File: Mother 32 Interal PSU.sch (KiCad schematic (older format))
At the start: 15 parts, among them P1 CONN_01X02, P2 CONN_02X08, P3 CONN_02X08, P4 CONN_02X08, P5 CONN_02X08, P6 CONN_02X08, P7 CONN_02X08, P8 CONN_02X08, P9 CONN_02X08, U1 BPM15, U2 R-78E5.0-0.5

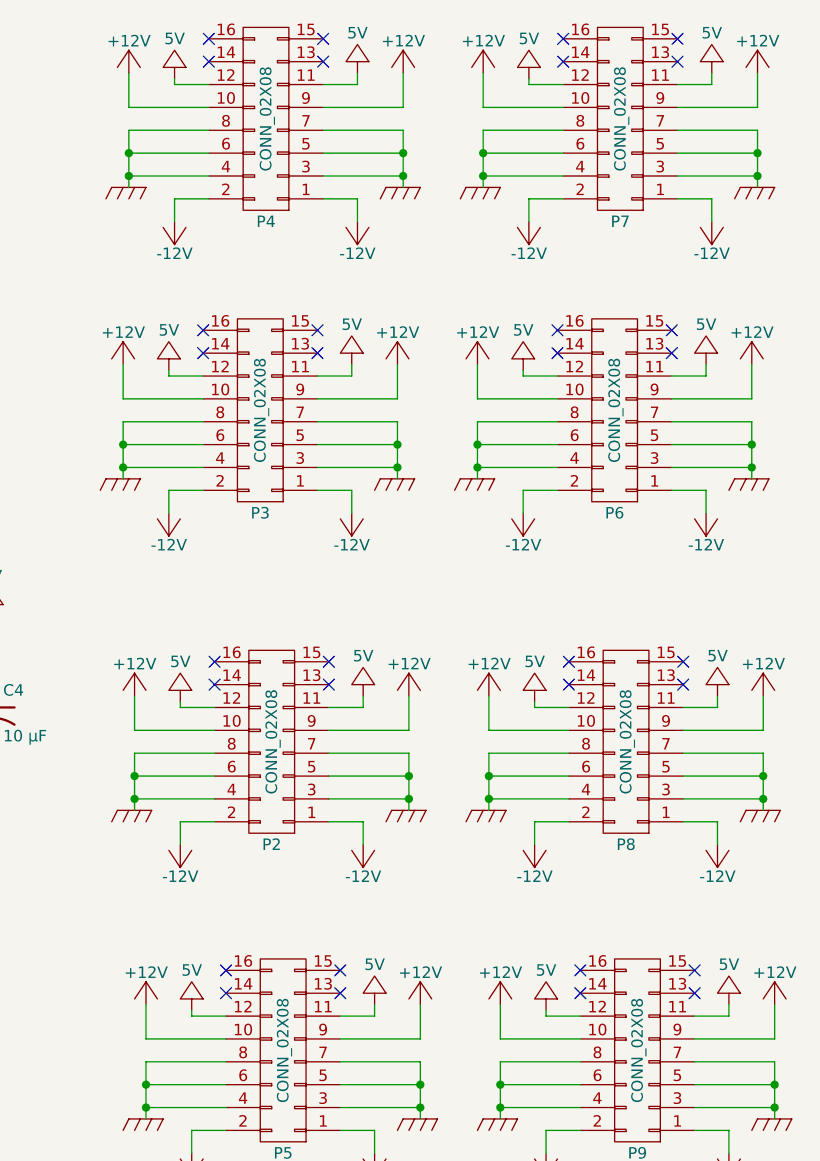
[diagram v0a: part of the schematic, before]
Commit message: updated ground planes and power traces, added CV/GATE connections
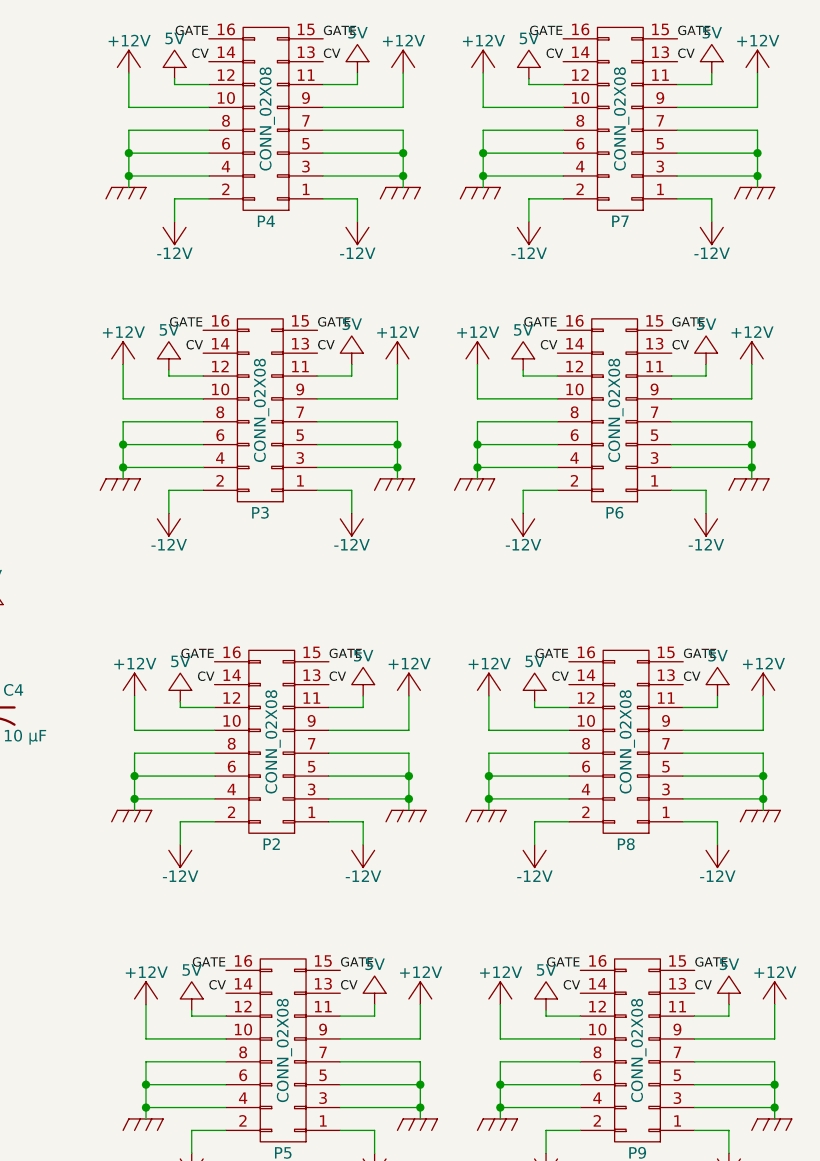
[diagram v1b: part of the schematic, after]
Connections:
- net CV: now reaches P2.13 (P13)
- net CV: now also P2.14 (P14), P3.13 (P13), P3.14 (P14), P4.13 (P13), P4.14 (P14), P5.13 (P13), P5.14 (P14), P6.13 (P13), P6.14 (P14), P7.13 (P13), P7.14 (P14), P8.13 (P13), P8.14 (P14), P9.13 (P13), P9.14 (P14)
- net GATE: now reaches P2.15 (P15)
- net GATE: now also P2.16 (P16), P3.15 (P15), P3.16 (P16), P4.15 (P15), P4.16 (P16), P5.15 (P15), P5.16 (P16), P6.15 (P15), P6.16 (P16), P7.15 (P15), P7.16 (P16), P8.15 (P15), P8.16 (P16), P9.15 (P15), P9.16 (P16)
- no-connect marks 32 -> 0
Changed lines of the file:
@@
 LIBS:valves
 LIBS:MySynthParts
+LIBS:Mother 32 Interal PSU-cache
 EELAYER 25 0
 EELAYER END
@@
 	1    0    0    -1
 $EndComp
-NoConn ~ 6575 3525
-NoConn ~ 6575 3625
-NoConn ~ 7075 3525
-NoConn ~ 7075 3625
 Wire Wire Line
 	6425 3700 6425 3725
@@
 	1    0    0    -1
 $EndComp
-NoConn ~ 8125 3525
-NoConn ~ 8125 3625
-NoConn ~ 8625 3525
-NoConn ~ 8625 3625
 Wire Wire Line
 	7975 3700 7975 3725
@@
 	1    0    0    -1
 $EndComp
-NoConn ~ 6525 2075
-NoConn ~ 6525 2175
-NoConn ~ 7025 2075
-NoConn ~ 7025 2175
 Wire Wire Line
 	6375 2250 6375 2275
@@
 	1    0    0    -1
 $EndComp
-NoConn ~ 8075 2075
-NoConn ~ 8075 2175
-NoConn ~ 8575 2075
-NoConn ~ 8575 2175
 Wire Wire Line
 	7925 2250 7925 2275
@@
 	1    0    0    -1
 $EndComp
-NoConn ~ 6625 4875
-NoConn ~ 6625 4975
-NoConn ~ 7125 4875
-NoConn ~ 7125 4975
 Wire Wire Line
 	6475 5050 6475 5075
@@
 	1    0    0    -1
 $EndComp
-NoConn ~ 8175 4875
-NoConn ~ 8175 4975
-NoConn ~ 8675 4875
-NoConn ~ 8675 4975
 Wire Wire Line
 	8025 5050 8025 5075
@@
 	1    0    0    -1
 $EndComp
-NoConn ~ 6550 800
-NoConn ~ 6550 900
-NoConn ~ 7050 800
-NoConn ~ 7050 900
 Wire Wire Line
 	6400 975  6400 1000
@@
 	1    0    0    -1
 $EndComp
-NoConn ~ 8100 800
-NoConn ~ 8100 900
-NoConn ~ 8600 800
-NoConn ~ 8600 900
 Wire Wire Line
 	7950 975  7950 1000
@@
 Wire Wire Line
 	8750 1500 8600 1500
+Text Label 7050 800  0    40   ~ 0
+GATE
+Text Label 6550 800  2    40   ~ 0
+GATE
+Text Label 8100 800  2    40   ~ 0
+GATE
+Text Label 8600 800  0    40   ~ 0
+GATE
+Text Label 6525 2075 2    40   ~ 0
+GATE
+Text Label 7025 2075 0    40   ~ 0
+GATE
+Text Label 8575 2075 0    40   ~ 0
+GATE
+Text Label 8075 2075 2    40   ~ 0
+GATE
+Text Label 6575 3525 2    40   ~ 0
+GATE
+Text Label 7075 3525 0    40   ~ 0
+GATE
+Text Label 8625 3525 0    40   ~ 0
+GATE
+Text Label 8125 3525 2    40   ~ 0
+GATE
+Text Label 6625 4875 2    40   ~ 0
+GATE
+Text Label 7125 4875 0    40   ~ 0
+GATE
+Text Label 8675 4875 0    40   ~ 0
+GATE
+Text Label 8175 4875 2    40   ~ 0
+GATE
+Text Label 6625 4975 2    40   ~ 0
+CV
+Text Label 7125 4975 0    40   ~ 0
+CV
+Text Label 8675 4975 0    40   ~ 0
+CV
+Text Label 8175 4975 2    40   ~ 0
+CV
+Text Label 6575 3625 2    40   ~ 0
+CV
+Text Label 7075 3625 0    40   ~ 0
+CV
+Text Label 8125 3625 2    40   ~ 0
+CV
+Text Label 8625 3625 0    40   ~ 0
+CV
+Text Label 8575 2175 0    40   ~ 0
+CV
+Text Label 8075 2175 2    40   ~ 0
+CV
+Text Label 7025 2175 0    40   ~ 0
+CV
+Text Label 6525 2175 2    40   ~ 0
+CV
+Text Label 8600 900  0    40   ~ 0
+CV
+Text Label 8100 900  2    40   ~ 0
+CV
+Text Label 7050 900  0    40   ~ 0
+CV
+Text Label 6550 900  2    40   ~ 0
+CV
 $EndSCHEMATC

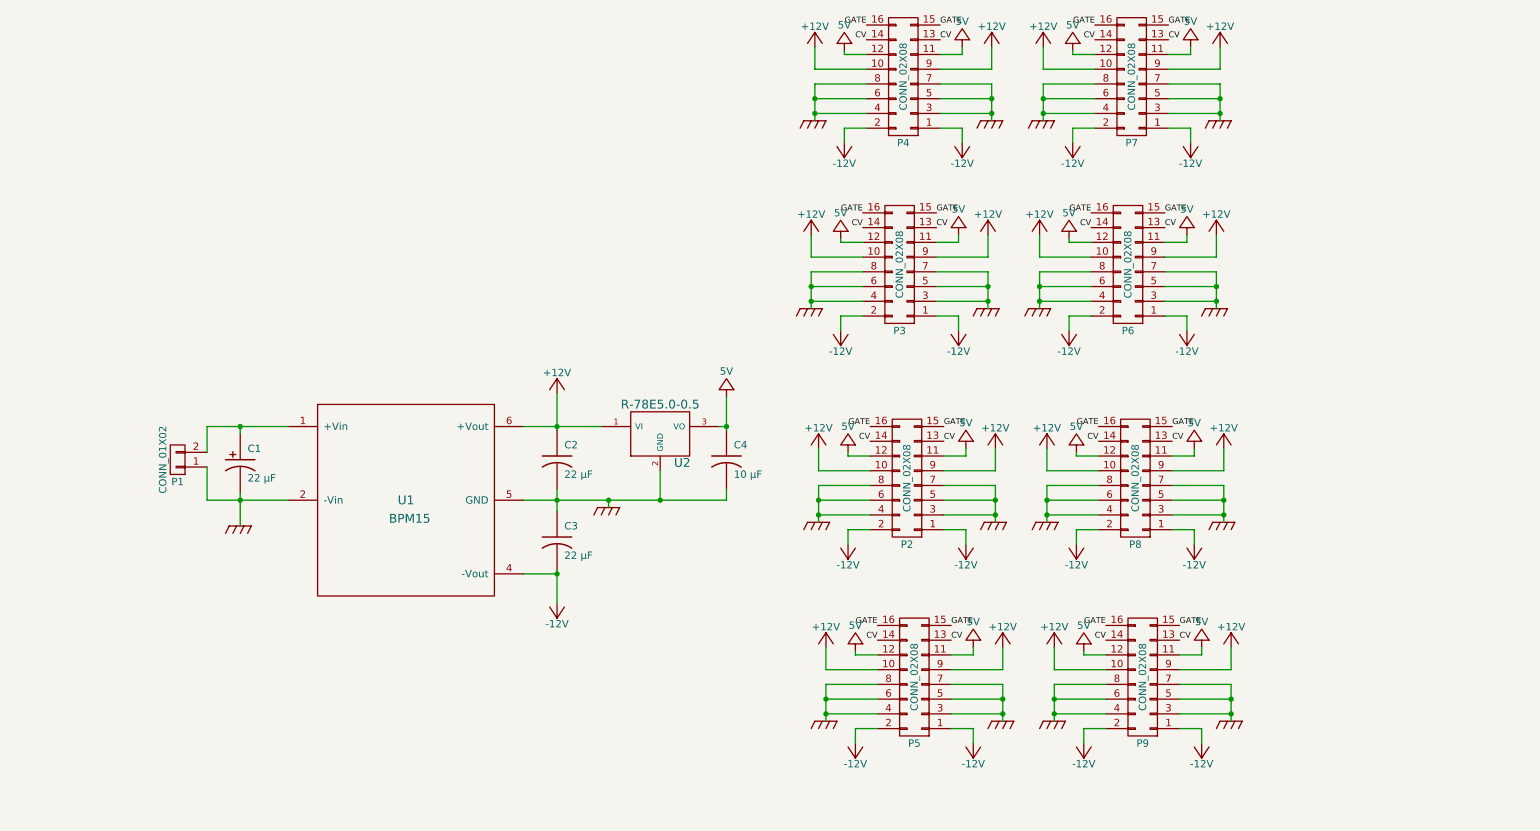
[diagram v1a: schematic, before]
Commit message: first commit with LDOs but these things will just get too damn hot, so will now revert to just LC filter on output
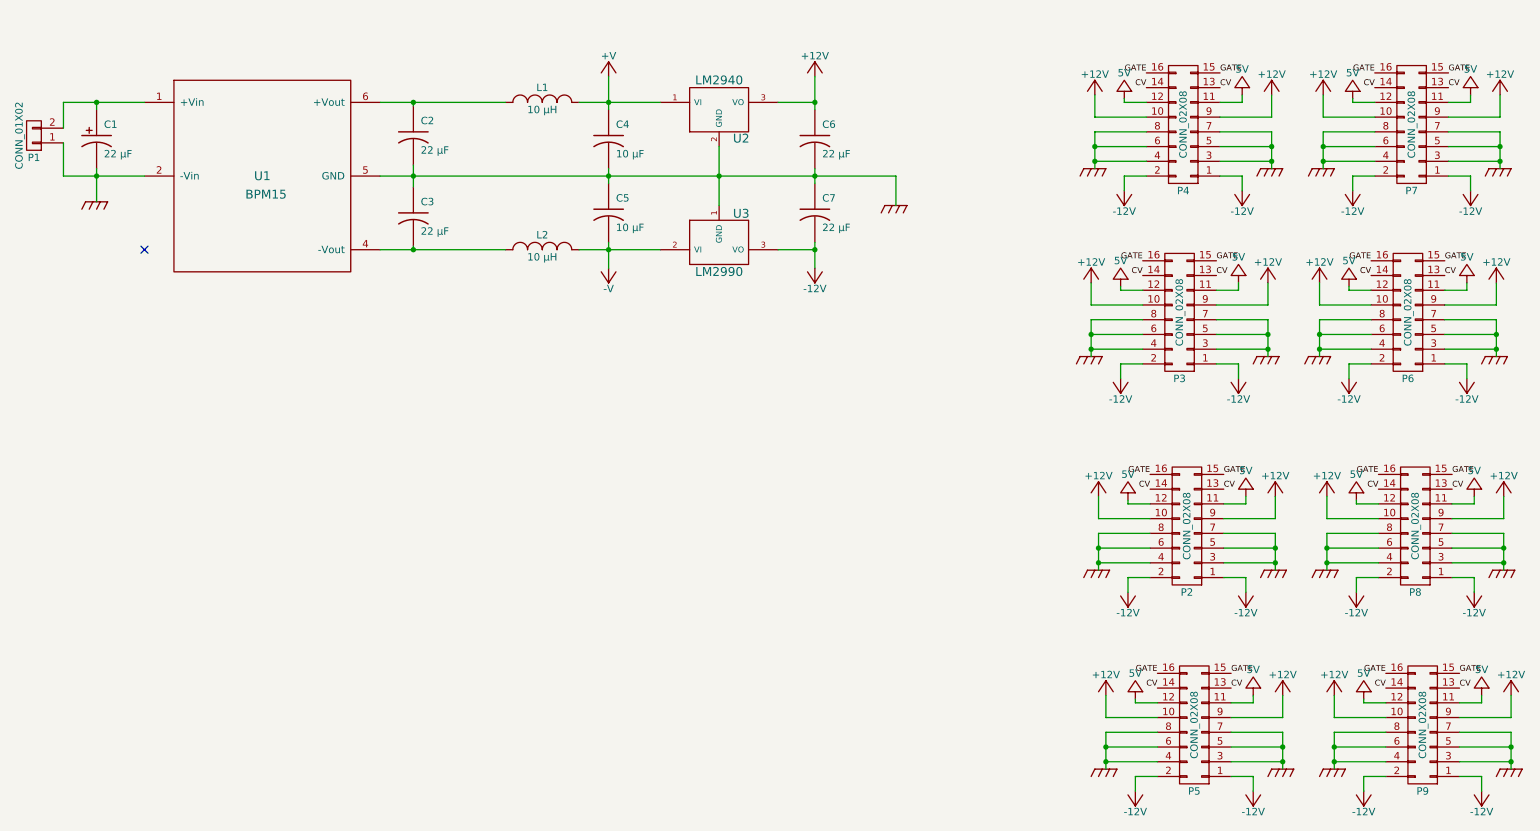
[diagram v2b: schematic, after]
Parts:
- removed U2: R-78E5.0-0.5, MyModules:R-78E-0.5, symbol R-78E5.0-1.0
- added C5: 10 μF, Capacitors_SMD:C_1206, symbol C_US
- added C6, C7: 22 μF, Capacitors_SMD:C_1210_HandSoldering, symbol C_US
- added L1, L2: 10 μH, Inductors_SMD:L_Taiyo-Yuden_NR-60xx_HandSoldering, symbol INDUCTOR_SMALL
- added U2: LM2940, TO_SOT_Packages_SMD:TO-263-3_TabPin2, symbol LM2940
- added U3: LM2990, TO_SOT_Packages_SMD:TO-263-3_TabPin2, symbol LM2990
- C2, C3: footprint Capacitors_SMD:C_1206 -> Capacitors_SMD:C_1210_HandSoldering
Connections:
- net +12V: now also C6.1, U2.3 (VO); no longer C2.1, U1.6 (+Vout)
- net +5V: no longer C4.1
- net -12V: now also C7.2, U3.3 (VO); no longer C3.2, U1.4 (-Vout)
- net GND: now also C5.1, C6.2, C7.1, U2.2 (GND), U3.1 (GND)
- new net: C3.2, L2.1, U1.4 (-Vout)
- new net: C2.1, L1.1, U1.6 (+Vout)
- new net +V: C4.1, L1.2, U2.1 (VI)
- new net -V: C5.2, L2.2, U3.2 (VI)
- no-connect marks 0 -> 1
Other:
- moved on the sheet: C1, C2, C3, C4, P1, P2, P3, P4, P5, P6, P7, P8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

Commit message: added LC filter to outputs
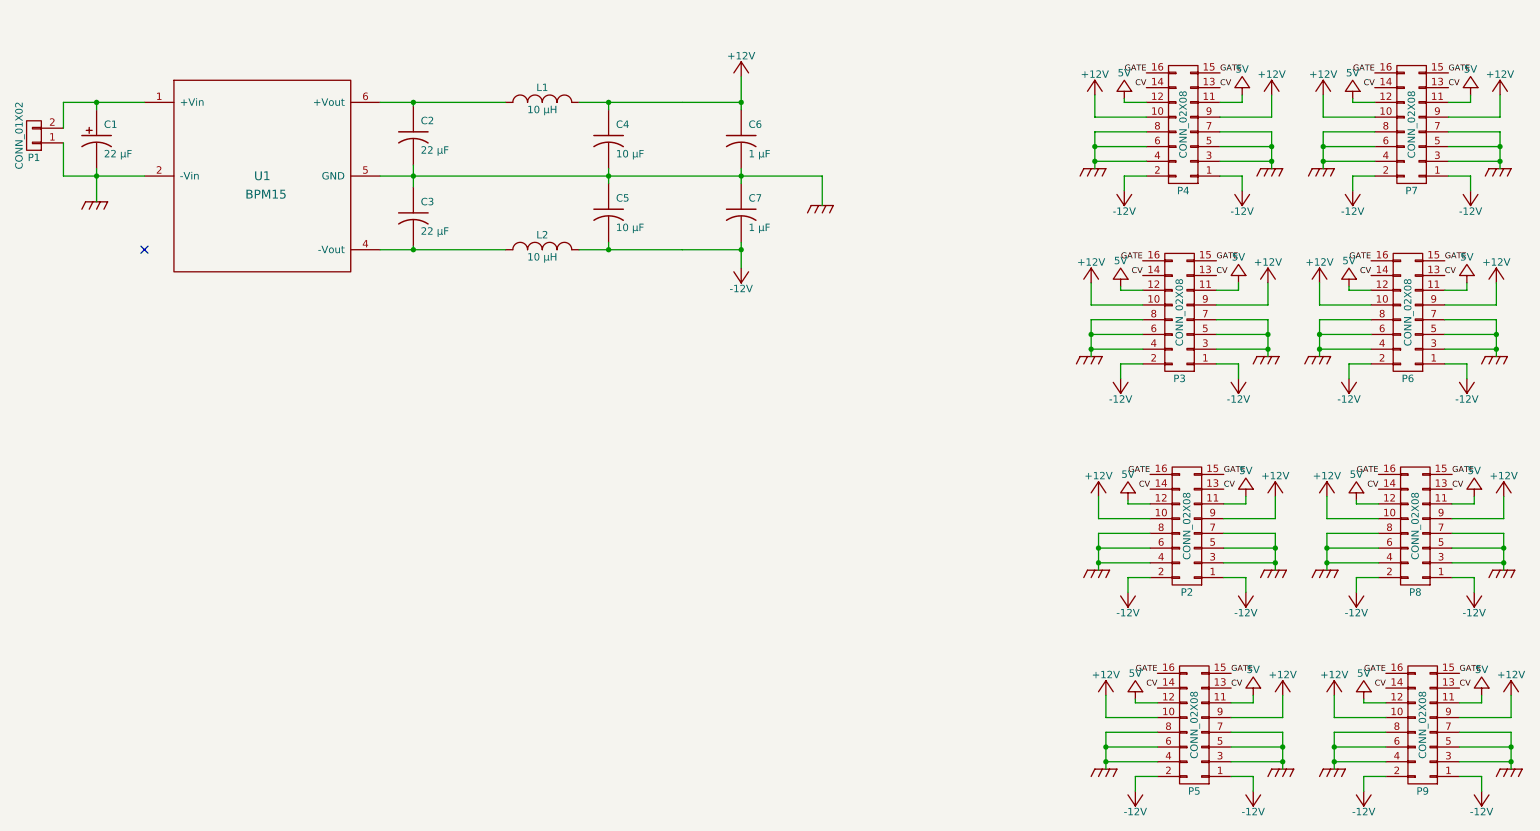
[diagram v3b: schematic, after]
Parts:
- removed U2: LM2940, TO_SOT_Packages_SMD:TO-263-3_TabPin2, symbol LM2940
- removed U3: LM2990, TO_SOT_Packages_SMD:TO-263-3_TabPin2, symbol LM2990
- C6, C7: value 22 μF -> 1 μF; footprint Capacitors_SMD:C_1210_HandSoldering -> Capacitors_SMD:C_0805
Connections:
- net +V is gone; now on net +12V: C4.1, L1.2
- net -V is gone; now on net -12V: C5.2, L2.2
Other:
- moved on the sheet: C6, C7

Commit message: LC filter added to output
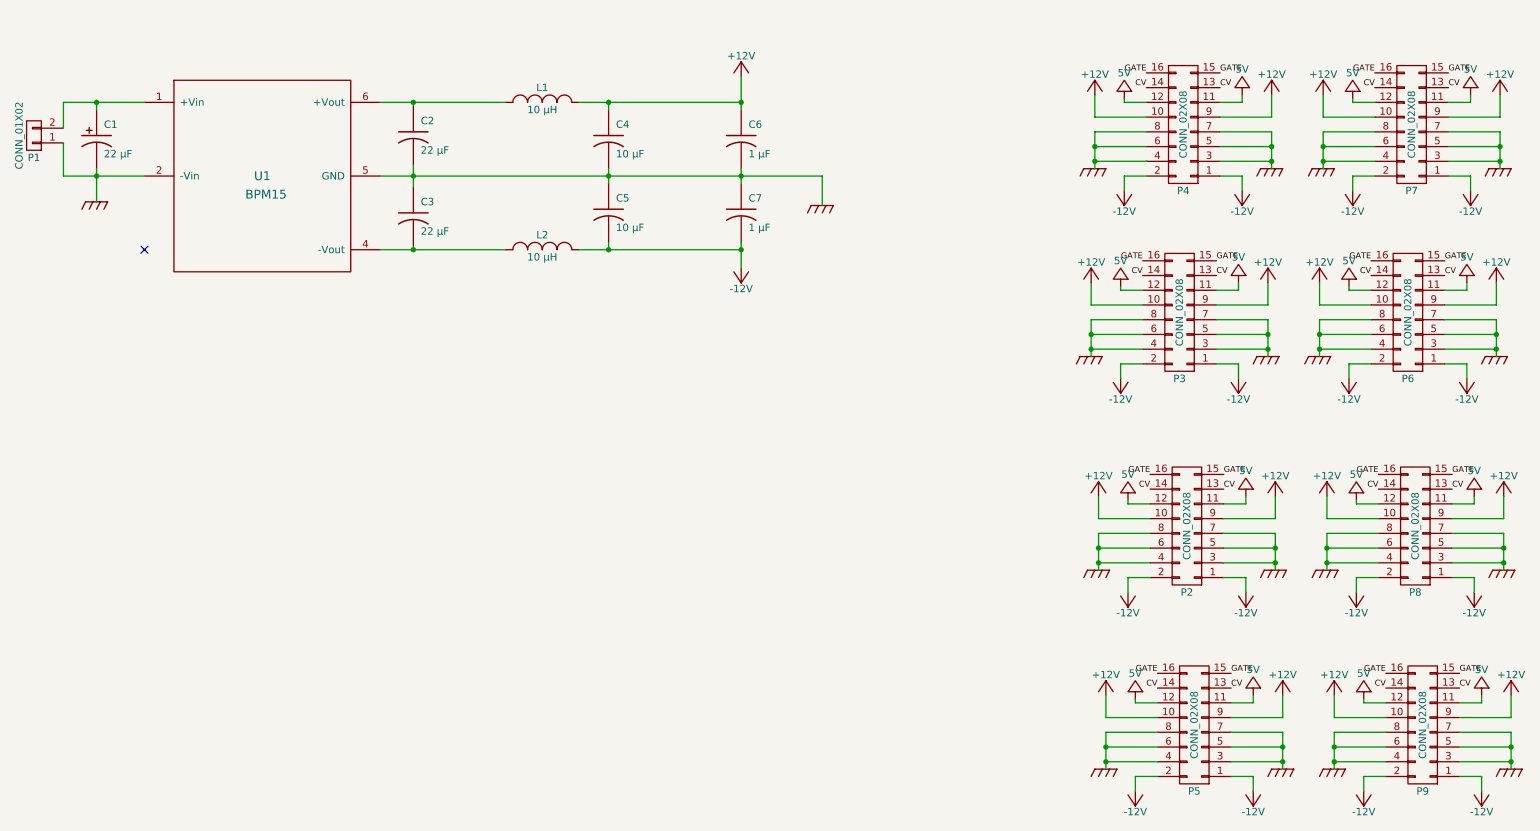
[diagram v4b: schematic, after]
